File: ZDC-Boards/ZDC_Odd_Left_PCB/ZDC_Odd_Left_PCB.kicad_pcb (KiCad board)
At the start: 2 copper layers, 178.2 x 643 mm, 73 parts

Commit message: Updated ZDC connectors to pad connections, v2.0
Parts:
- removed REF**: PinHeader_2x25_P1.27mm_Horizontal, Connector_PinHeader_1.27mm:PinHeader_2x25_P1.27mm_Horizontal
- removed REF**: PinHeader_2x15_P1.27mm_Horizontal, Connector_PinHeader_1.27mm:PinHeader_2x15_P1.27mm_Horizontal
- added J1: TE_5-104895-3_AMPMODU_50-50_2x15_P1.27mm_Horizontal_SMD, TE_AMPMODU:TE_5-104895-3_AMPMODU_50-50_2x15_P1.27mm_Horizontal_SMD, F.Cu at (56.3, -634.4)
- added J2: TE_5-104895-5_AMPMODU_50-50_2x25_P1.27mm_Horizontal_SMD, TE_AMPMODU:TE_5-104895-5_AMPMODU_50-50_2x25_P1.27mm_Horizontal_SMD, F.Cu at (146.4, -634.4)
- #MK1, #MK2: renamed from REF**20; footprint SiPM:S14160-1315PS_dimple_silkscreen_with_capacitor -> SiPM:S14160-1315PS_silkscreen_marker
- C0, C1, C10, C11, C12, C13, C14, C15, C16, C17, C18, C19, C2, C20, C21, C22, C23, C24, C25, C26, C27, C28, C29, C3, C30, C31, C32, C4, C5, C6, C7, C8, C9: renamed from 10 nF
- renumbered REF**20 to D0, REF**20 to D1, REF**20 to D10, REF**20 to D11, REF**20 to D12, REF**20 to D13, REF**20 to D14, REF**20 to D15, REF**20 to D16, REF**20 to D17, REF**20 to D18, REF**20 to D19, REF**20 to D2, REF**20 to D20, REF**20 to D21, REF**20 to D22, REF**20 to D23, REF**20 to D24, REF**20 to D25, REF**20 to D26, REF**20 to D27, REF**20 to D28, REF**20 to D29, REF**20 to D3, REF**20 to D30, REF**20 to D31, REF**20 to D32, REF**20 to D4, REF**20 to D5, REF**20 to D6, REF**20 to D7, REF**20 to D8, REF**20 to D9, REF** to J3, REF** to J4
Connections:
- C0 pad 1: K12 -> K0
- C1 pad 1: K13 -> K1
- C10 pad 1: K22 -> K10
- C11 pad 1: K0 -> K11
- C12 pad 1: K1 -> K12
- C13 pad 1: K2 -> K13
- C14 pad 1: K3 -> K14
- C15 pad 1: K4 -> K15
- C16 pad 1: K5 -> K16
- C17 pad 1: K6 -> K17
- C18 pad 1: K7 -> K18
- C19 pad 1: K8 -> K19
- C2 pad 1: K14 -> K2
- C20 pad 1: K9 -> K20
- C21 pad 1: K10 -> K21
- C22 pad 1: K12 -> K22
- C23 pad 1: K13 -> K23
- C24 pad 1: K14 -> K24
- C25 pad 1: K15 -> K25
- C26 pad 1: K16 -> K26
- C27 pad 1: K17 -> K27
- C28 pad 1: K18 -> K28
- C29 pad 1: K19 -> K29
- C3 pad 1: K15 -> K3
- C30 pad 1: K20 -> K30
- C31 pad 1: K21 -> K31
- C32 pad 1: K22 -> K32
- C4 pad 1: K16 -> K4
- C5 pad 1: K17 -> K5
- C6 pad 1: K18 -> K6
- C7 pad 1: K19 -> K7
- C8 pad 1: K20 -> K8
- C9 pad 1: K21 -> K9
- D0 pad : LK -> LK1
- D0 pad 7: K12 -> K0
- D0 pad 8: A12 -> A0
- D0 pad 9: LA -> LA1
- D1 pad : LK -> LK1
- D1 pad 7: (no net) -> K1
- D1 pad 8: (no net) -> A1
- D1 pad 9: LA -> LA1
- D10 pad : LK -> LK1
- D10 pad 7: (no net) -> K10
- D10 pad 8: (no net) -> A10
- D10 pad 9: LA -> LA1
- D11 pad : LK -> LK2
- D11 pad 7: (no net) -> K11
- D11 pad 8: (no net) -> A11
- D11 pad 9: LA -> LA2
- D12 pad : LK -> LK2
- D12 pad 7: (no net) -> K12
- D12 pad 8: (no net) -> A12
- D12 pad 9: LA -> LA2
- D13 pad : LK -> LK2
- D13 pad 7: (no net) -> K13
- D13 pad 8: (no net) -> A13
- D13 pad 9: LA -> LA2
- D14 pad : LK -> LK2
- D14 pad 7: (no net) -> K14
- D14 pad 8: (no net) -> A14
- D14 pad 9: LA -> LA2
- D15 pad : LK -> LK2
- D15 pad 7: (no net) -> K15
- D15 pad 8: (no net) -> A15
- D15 pad 9: LA -> LA2
- D16 pad : LK -> LK2
- D16 pad 7: (no net) -> K16
- D16 pad 8: A5 -> A16
- D16 pad 9: LA -> LA2
- D17 pad : LK -> LK2
- D17 pad 7: (no net) -> K17
- D17 pad 8: (no net) -> A17
- D17 pad 9: LA -> LA2
- D18 pad : LK -> LK2
- D18 pad 7: (no net) -> K18
- D18 pad 8: (no net) -> A18
- D18 pad 9: LA -> LA2
- D19 pad : LK -> LK2
- D19 pad 7: (no net) -> K19
- D19 pad 8: (no net) -> A19
- D19 pad 9: LA -> LA2
- D2 pad : LK -> LK1
- D2 pad 7: (no net) -> K2
- D2 pad 8: (no net) -> A2
- D2 pad 9: LA -> LA1
- D20 pad : LK -> LK2
- D20 pad 7: (no net) -> K20
- D20 pad 8: (no net) -> A20
- D20 pad 9: LA -> LA2
- D21 pad : LK -> LK2
- D21 pad 7: (no net) -> K21
- D21 pad 8: (no net) -> A21
- D21 pad 9: LA -> LA2
- D22 pad : LK -> LK2
- D22 pad 7: K12 -> K22
- D22 pad 8: A12 -> A22
- D22 pad 9: LA -> LA2
- D23 pad : LK -> LK2
- D23 pad 7: (no net) -> K23
- D23 pad 8: (no net) -> A23
- D23 pad 9: LA -> LA2
- D24 pad : LK -> LK2
- D24 pad 7: (no net) -> K24
- D24 pad 8: (no net) -> A24
- D24 pad 9: LA -> LA2
- D25 pad : LK -> LK2
- D25 pad 7: (no net) -> K25
- D25 pad 8: (no net) -> A25
- D25 pad 9: LA -> LA2
- D26 pad : LK -> LK2
- D26 pad 7: (no net) -> K26
- D26 pad 8: (no net) -> A26
- D26 pad 9: LA -> LA2
- D27 pad : LK -> LK2
- D27 pad 7: (no net) -> K27
- D27 pad 8: A17 -> A27
- D27 pad 9: LA -> LA2
- D28 pad : LK -> LK2
- D28 pad 7: (no net) -> K28
- D28 pad 8: (no net) -> A28
- D28 pad 9: LA -> LA2
- D29 pad : LK -> LK2
- D29 pad 7: (no net) -> K29
- D29 pad 8: (no net) -> A29
- D29 pad 9: LA -> LA2
- D3 pad : LK -> LK1
- D3 pad 7: (no net) -> K3
- D3 pad 8: (no net) -> A3
- D3 pad 9: LA -> LA1
- D30 pad : LK -> LK2
- D30 pad 7: (no net) -> K30
- D30 pad 8: (no net) -> A30
- D30 pad 9: LA -> LA2
- D31 pad : LK -> LK2
- D31 pad 7: (no net) -> K31
- D31 pad 8: (no net) -> A31
- D31 pad 9: LA -> LA2
- D32 pad : LK -> LK2
- D32 pad 7: (no net) -> K32
- D32 pad 8: (no net) -> A32
- D32 pad 9: LA -> LA2
- D4 pad : LK -> LK1
- D4 pad 7: (no net) -> K4
- D4 pad 8: (no net) -> A4
- D4 pad 9: LA -> LA1
- D5 pad : LK -> LK1
- D5 pad 7: (no net) -> K5
- D5 pad 8: A17 -> A5
- D5 pad 9: LA -> LA1
- D6 pad : LK -> LK1
- D6 pad 7: (no net) -> K6
- D6 pad 8: (no net) -> A6
- D6 pad 9: LA -> LA1
- D7 pad : LK -> LK1
- D7 pad 7: (no net) -> K7
- D7 pad 8: (no net) -> A7
- D7 pad 9: LA -> LA1
- D8 pad : LK -> LK1
- D8 pad 7: (no net) -> K8
- D8 pad 8: (no net) -> A8
- D8 pad 9: LA -> LA1
- D9 pad : LK -> LK1
- D9 pad 7: (no net) -> K9
- D9 pad 8: (no net) -> A9
- D9 pad 9: LA -> LA1
- J3 pad 1: LA -> LA1
- J3 pad 2: LK -> LK1
- J4 pad 1: LA -> LA2
- J4 pad 2: LK -> LK2
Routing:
- net LK: track 1838.9 -> 0.00 mm, vias 33 -> 0
- net LA: track 1754.5 -> 0.00 mm, vias 1 -> 0
- net LK2: track 0.00 -> 1189.8 mm, vias 0 -> 22
- net LA2: track 0.00 -> 1141.6 mm, vias 0 -> 1
- net K22: track 1235.9 -> 128.7 mm, vias 4 -> 2
- net A22: track 1268.0 -> 169.3 mm
- net LK1: track 0.00 -> 649.1 mm, vias 0 -> 11
- net A32: track 0.00 -> 634.3 mm
- net K32: track 0.00 -> 618.5 mm, vias 0 -> 2
- net LA1: track 0.00 -> 614.2 mm
- net A31: track 0.00 -> 588.9 mm
- net K31: track 0.00 -> 570.2 mm, vias 0 -> 2
- net A21: track 1174.1 -> 631.3 mm
- net A30: track 0.00 -> 542.2 mm
- net K21: track 1139.8 -> 597.7 mm, vias 4 -> 2
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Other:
- board text added: "TE 5-104895-3 (AMPMODU 50/50 R/A SMT)"
- board text added: "TE 5-104895-5 (AMPMODU 50/50 R/A SMT)"
- board text added: "ZDC Odd Left PCB v2.0 Designed by Sean Preins"
- board text removed: "PinHeader_2x25_P1.27mm_Horizontal"
- board text removed: "ZDC Odd Left PCB v1.0 Designed by Sean Preins"

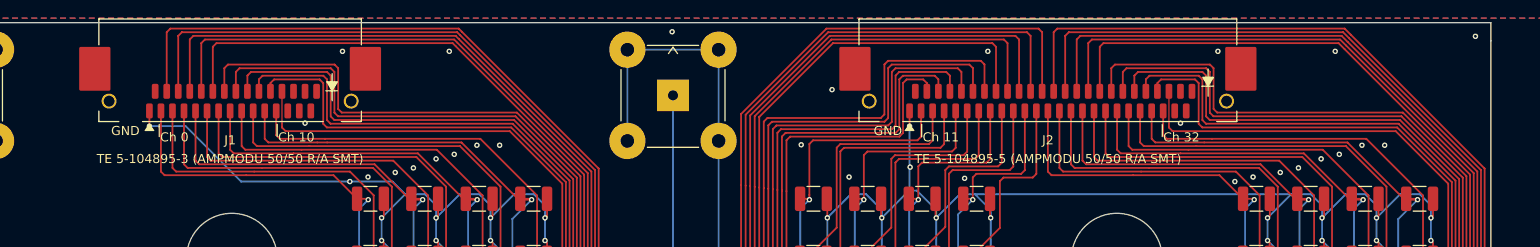
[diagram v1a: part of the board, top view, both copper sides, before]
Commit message: Updated ZDC boards to use new pin connectors that attach to crimped cables
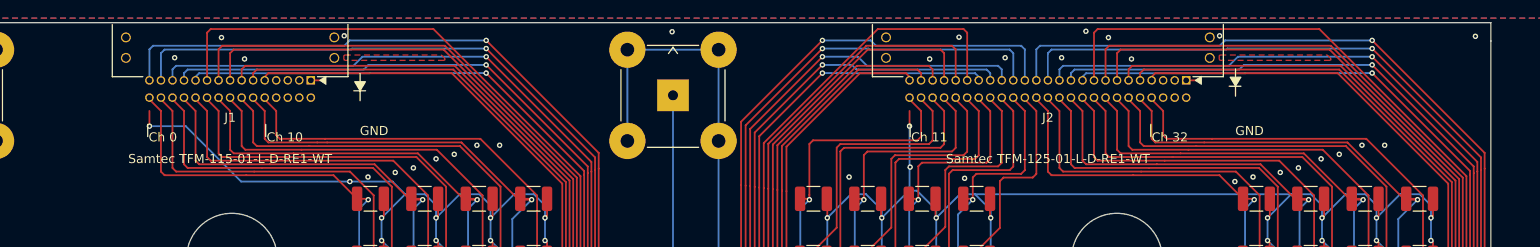
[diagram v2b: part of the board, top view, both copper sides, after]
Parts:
- J1: value TE_5-104895-3_AMPMODU_50-50_2x15_P1.27mm_Horizontal_SMD -> Samtec_TFM-115-01-x-D-RE1-WT_2x15_P1.27mm_Horizontal; footprint TE_AMPMODU:TE_5-104895-3_AMPMODU_50-50_2x15_P1.27mm_Horizontal_SMD -> Samtec_TFM:Samtec_TFM-115-01-x-D-RE1-WT_2x15_P1.27mm_Horizontal
- J2: value TE_5-104895-5_AMPMODU_50-50_2x25_P1.27mm_Horizontal_SMD -> Samtec_TFM-125-01-x-D-RE1-WT_2x25_P1.27mm_Horizontal; footprint TE_AMPMODU:TE_5-104895-5_AMPMODU_50-50_2x25_P1.27mm_Horizontal_SMD -> Samtec_TFM:Samtec_TFM-125-01-x-D-RE1-WT_2x25_P1.27mm_Horizontal
- moved #MK1 3.08 mm to (70.6, -635.5)
- moved #MK2 3.02 mm to (167.0, -636.0)
- moved J1 1.34 mm to (56.3, -635.7), turned to 0 degrees
- moved J2 1.34 mm to (146.4, -635.7), turned to 0 degrees
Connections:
- J1 pad 10: A3 -> K10
- J1 pad 11: K4 -> A9
- J1 pad 12: A4 -> K9
- J1 pad 13: K5 -> A8
- J1 pad 14: A5 -> K8
- J1 pad 15: K6 -> A7
- J1 pad 16: A6 -> K7
- J1 pad 17: K7 -> A6
- J1 pad 18: A7 -> K6
- J1 pad 19: K8 -> A5
- J1 pad 20: A8 -> K5
- J1 pad 21: K9 -> A4
- J1 pad 22: A9 -> K4
- J1 pad 23: K10 -> A3
- J1 pad 24: A10 -> K3
- J1 pad 25: (no net) -> A2
- J1 pad 26: (no net) -> K2
- J1 pad 27: (no net) -> A1
- J1 pad 28: (no net) -> K1
- J1 pad 29: (no net) -> A0
- J1 pad 3: K0 -> (no net)
- J1 pad 30: (no net) -> K0
- J1 pad 4: A0 -> (no net)
- J1 pad 5: K1 -> (no net)
- J1 pad 6: A1 -> (no net)
- J1 pad 7: K2 -> (no net)
- J1 pad 8: A2 -> (no net)
- J1 pad 9: K3 -> A10
- J1 pad MP: (no net) -> GND
- J2 pad 10: A14 -> K31
- J2 pad 11: K15 -> A30
- J2 pad 12: A15 -> K30
- J2 pad 13: K16 -> A29
- J2 pad 14: A16 -> K29
- J2 pad 15: K17 -> A28
- J2 pad 16: A17 -> K28
- J2 pad 17: K18 -> A27
- J2 pad 18: A18 -> K27
- J2 pad 19: K19 -> A26
- J2 pad 20: A19 -> K26
- J2 pad 21: K20 -> A25
- J2 pad 22: A20 -> K25
- J2 pad 23: K21 -> A24
- J2 pad 24: A21 -> K24
- J2 pad 25: K22 -> A23
- J2 pad 26: A22 -> K23
- J2 pad 27: K23 -> A22
- J2 pad 28: A23 -> K22
- J2 pad 29: K24 -> A21
- J2 pad 3: K11 -> (no net)
- J2 pad 30: A24 -> K21
- J2 pad 31: K25 -> A20
- J2 pad 32: A25 -> K20
- J2 pad 33: K26 -> A19
- J2 pad 34: A26 -> K19
- J2 pad 35: K27 -> A18
- J2 pad 36: A27 -> K18
- J2 pad 37: K28 -> A17
- J2 pad 38: A28 -> K17
- J2 pad 39: K29 -> A16
- J2 pad 4: A11 -> (no net)
- J2 pad 40: A29 -> K16
- J2 pad 41: K30 -> A15
- J2 pad 42: A30 -> K15
- J2 pad 43: K31 -> A14
- J2 pad 44: A31 -> K14
- J2 pad 45: K32 -> A13
- J2 pad 46: A32 -> K13
- J2 pad 47: (no net) -> A12
- J2 pad 48: (no net) -> K12
- J2 pad 49: (no net) -> A11
- J2 pad 5: K12 -> (no net)
- J2 pad 50: (no net) -> K11
- J2 pad 6: A12 -> (no net)
- J2 pad 7: K13 -> A32
- J2 pad 8: A13 -> K32
- J2 pad 9: K14 -> A31
- J2 pad MP: (no net) -> GND
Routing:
- net A17: track 425.7 -> 416.7 mm, vias 0 -> 1
- net A18: track 477.1 -> 468.7 mm, vias 0 -> 1
- net A19: track 528.5 -> 520.7 mm, vias 0 -> 1
- net A20: track 579.9 -> 573.5 mm, vias 0 -> 1
- net A13: track 220.3 -> 214.1 mm
- net A12: track 168.7 -> 162.7 mm
- net A21: track 631.3 -> 625.5 mm, vias 0 -> 1
- net A11: track 117.7 -> 112.0 mm
- net A15: track 323.5 -> 318.9 mm
- net A14: track 271.9 -> 267.5 mm
- net A26: track 355.5 -> 351.8 mm, vias 0 -> 1
- net A4: track 355.6 -> 351.9 mm, vias 0 -> 1
- net A27: track 402.1 -> 405.7 mm
- net A5: track 402.2 -> 405.8 mm
- net A3: track 308.9 -> 305.8 mm, vias 0 -> 1
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- added copper zone on F.Cu, net (none)
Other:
- board text added: "Samtec TFM-115-01-L-D-RE1-WT"
- board text added: "Samtec TFM-125-01-L-D-RE1-WT"
- board text removed: "TE 5-104895-3 (AMPMODU 50/50 R/A SMT)"
- board text removed: "TE 5-104895-5 (AMPMODU 50/50 R/A SMT)"
